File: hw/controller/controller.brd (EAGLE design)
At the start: 45 x 45 mm, 99 parts, among them J1 JST-PH3SMT_VERT, J2 JST-PH3SMT_VERT, M3 PAD24AWG_PAD, Q1 TPN1R603PL, Q2 TPN1R603PL, Q3 TPN1R603PL, Q4 TPN1R603PL, Q5 TPN1R603PL, Q6 TPN1R603PL, U1 STM32F4R_64PIN, U2 DRV8323RS, U3 AS5147, U4 MAX13431E, U5 MAX13433EETD+T, X1 8.0MHz

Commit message: controller: Officially switch to 500mOhm sense resistor
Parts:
- RA, RB, RC: value 1mOhm 1% 2W -> 0.5mOhm 1% 2W
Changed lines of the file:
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@@
 <attribute name="MF" value="Samsung Electro-Mechanics" x="26.9" y="25.9" size="1.778" layer="27" display="off"/>
 </element>
-<element name="RA" library="rcl" package="M1206" value="1mOhm 1% 2W" x="18.2" y="9.6" smashed="yes" rot="R270">
+<element name="RA" library="rcl" package="M1206" value="0.5mOhm 1% 2W" x="18.2" y="9.6" smashed="yes" rot="R270">
 <attribute name="MF" value="Stackpole Electronics" x="18.2" y="9.6" size="1.778" layer="27" rot="R270" display="off"/>
-<attribute name="MPN" value="HCS1206FT1L00" x="18.2" y="9.6" size="1.778" layer="27" rot="R270" display="off"/>
+<attribute name="MPN" value="HCS1206FTL500" x="18.2" y="9.6" size="1.778" layer="27" rot="R270" display="off"/>
 <attribute name="NAME" x="18.770003125" y="7.23" size="0.6096" layer="25" font="vector" ratio="10" rot="R180"/>
 <attribute name="POPULATE" value="1" x="18.2" y="9.6" size="1.778" layer="27" rot="R270" display="off"/>
@@
 <attribute name="POPULATE" value="0" x="33.63" y="12.03" size="1.778" layer="27" rot="R90" display="off"/>
 </element>
-<element name="RB" library="rcl" package="M1206" value="1mOhm 1% 2W" x="21.4" y="9.6" smashed="yes" rot="R270">
-<attribute name="MPN" value="HCS1206FT1L00" x="21.4" y="9.6" size="1.778" layer="27" rot="R270" display="off"/>
+<element name="RB" library="rcl" package="M1206" value="0.5mOhm 1% 2W" x="21.4" y="9.6" smashed="yes" rot="R270">
+<attribute name="MPN" value="HCS1206FTL500" x="21.4" y="9.6" size="1.778" layer="27" rot="R270" display="off"/>
 <attribute name="MF" value="Stackpole Electronics" x="21.4" y="9.6" size="1.778" layer="27" rot="R270" display="off"/>
 <attribute name="NAME" x="22.070003125" y="7.23" size="0.6096" layer="25" font="vector" ratio="10" rot="R180"/>
 <attribute name="POPULATE" value="1" x="21.4" y="9.6" size="1.778" layer="27" rot="R270" display="off"/>
 </element>
-<element name="RC" library="rcl" package="M1206" value="1mOhm 1% 2W" x="34.5" y="9.6" smashed="yes" rot="R270">
-<attribute name="MPN" value="HCS1206FT1L00" x="34.5" y="9.6" size="1.778" layer="27" rot="R270" display="off"/>
+<element name="RC" library="rcl" package="M1206" value="0.5mOhm 1% 2W" x="34.5" y="9.6" smashed="yes" rot="R270">
+<attribute name="MPN" value="HCS1206FTL500" x="34.5" y="9.6" size="1.778" layer="27" rot="R270" display="off"/>
 <attribute name="MF" value="Stackpole Electronics" x="34.5" y="9.6" size="1.778" layer="27" rot="R270" display="off"/>
 <attribute name="NAME" x="35.17" y="7.229996875" size="0.6096" layer="25" ratio="10" rot="R180"/>

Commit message: controller: Transcribe r3.1 part selection back into eagle
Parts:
- C12, C23, C24, C25, C27, C28, C29, C30: value 1uF 35V -> 1.5uF 35V

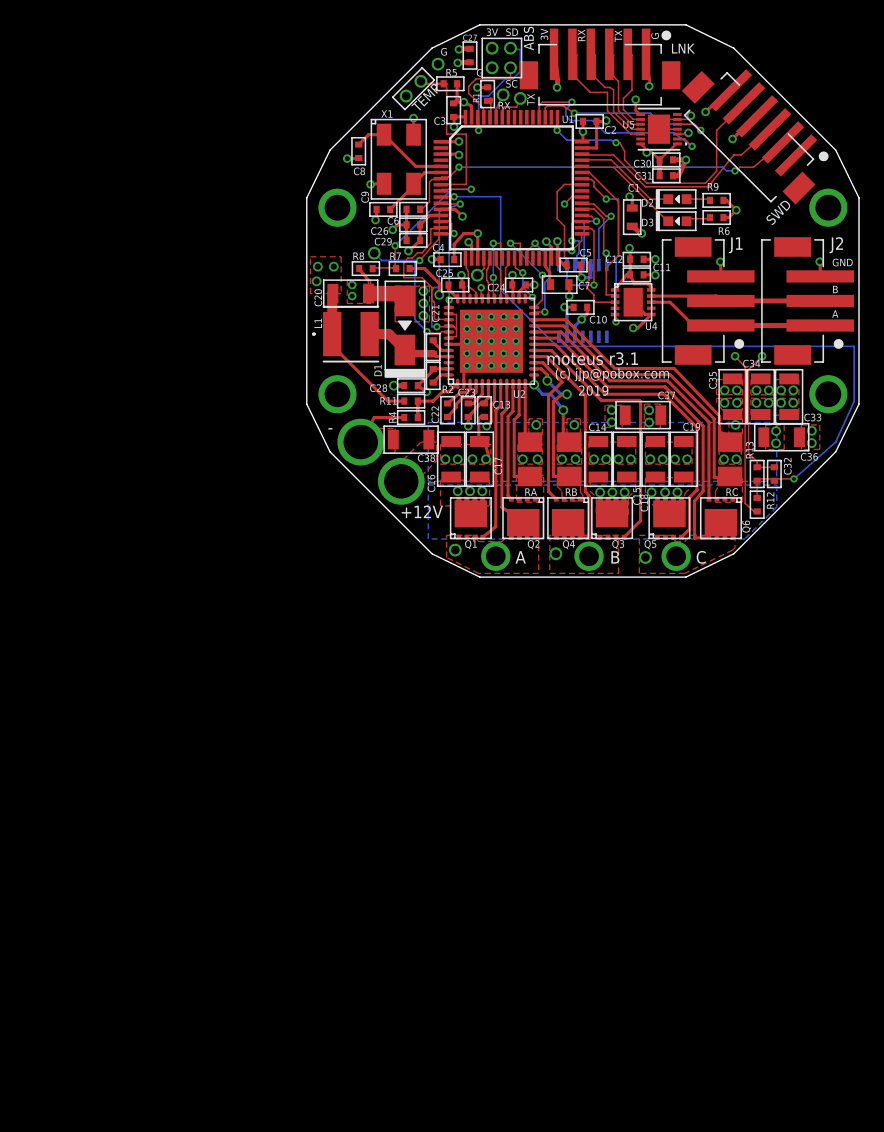
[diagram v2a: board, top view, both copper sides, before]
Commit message: Work on r4 of controller
Parts are in place, but part names are bogus, silks haven't been
placed, and auto-routing not done yet.
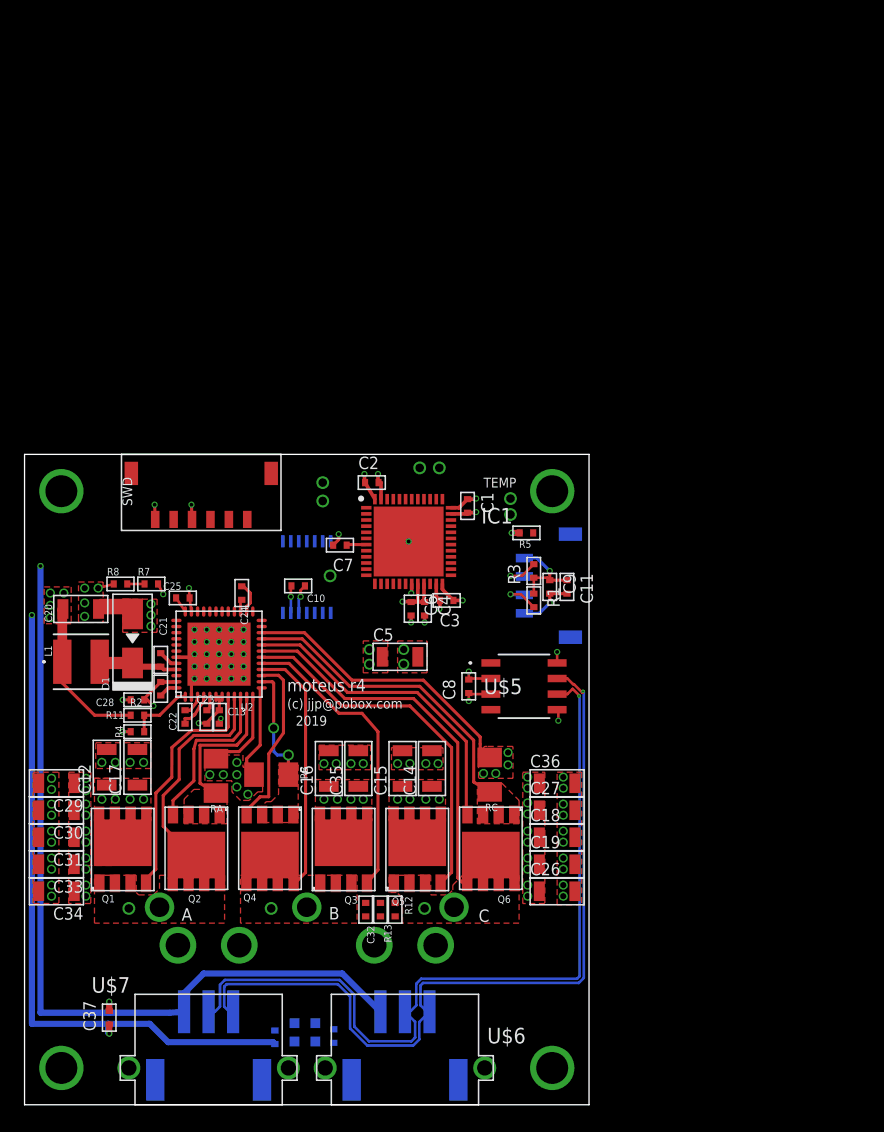
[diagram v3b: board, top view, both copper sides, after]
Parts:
- removed ABS_3V, ABS_GND, ABS_SCL, ABS_SDA, DAC1, DGND, DRX, DTX, M3: PAD24AWG_PAD, controller:24AWG_PAD
- removed C38: 10uF, mfpassives:C1206
- removed J1, J2: JST-PH3SMT_VERT, controller:JST_B3B_PH-SM4-TB(LF)(SN)
- removed LNK: JST-ZH6SMT_VERT, controller:JST_B6B-ZR-SM4-TF(LF)(SN)
- removed U1: STM32F4R_64PIN, controller:LQFP64
- removed U4: MAX13431E, controller:TDFN10
- removed U5: MAX13433EETD+T, controller:21-0137I_T1433-1
- removed V+, V-: PAD12AWG_PAD, controller:12AWG_PAD
- removed X1: 8.0MHz, controller:ABM3B
- added IC1: STM32G474CEU6, controller:QFN50P700X700X60-49N
- added R3: 2k, mfpassives:R0402
- added U$10, U$11: JST-PH3, controller:JST_S3B-PH-SM4-TB(LF)(SN)
- added U$12, U$13, U$14, U$9: MOUNT, controller:M2.5MOUNT
- added U$15: PAD24AWG_PAD, controller:24AWG_PAD
- added U$5: TCAN334G, controller:SOT23-8
- added U$6, U$7: XT30XT30PW_MALE, controller:XT30PW_MALE
- added U$8: JST_ZH4, controller:JST_S4B-ZR-SM4A-TF(LF)(SN)
- C1, C7: value 4.7uF -> 0.1uF 50V; device mfpassives:C0603 -> mfpassives:C0402
- C12, C27, C29, C30: value 1.5uF 35V -> 10uF; device mfpassives:C0402 -> mfpassives:C1206
- C26, C31, C5: value 0.1uF 50V -> 10uF; device mfpassives:C0402 -> mfpassives:C1206
- C37: value 10uF -> 0.1uF 50V; device mfpassives:C1206 -> mfpassives:C0402
- C6: value 0.1uF 50V -> 1uF
- C8: value 10pF -> 0.1uF 50V
- C9: value 10pF -> 1uF
- Q1, Q2, Q3, Q4, Q5, Q6: value TPN1R603PL -> TPH1R204PLSOP_ADVANCE_8; device controller:TSON_ADVANCE_8 -> controller:SOP_ADVANCE_8
- R1: value 220 -> 2k
- SWD: value JST-ZH6SMT_VERT -> JST-ZH6; device controller:JST_B6B-ZR-SM4-TF(LF)(SN) -> controller:JST_S6B-ZR-SM4A-TF(LF)(SN)
- U$1, U$2, U$3, U$4: value MOUNTM2 -> PAD24AWG_PAD; device controller:M2MOUNT -> controller:24AWG_PAD
- moved R6 75.9 mm to (-2.60, -37.5), flipped to the bottom, turned to 90 degrees
- moved R9 74.9 mm to (2.20, -37.4), flipped to the bottom, turned to 90 degrees
- moved D2 74.0 mm to (0.70, -37.1), flipped to the bottom, turned to 270 degrees
- moved C31 73.3 mm to (-20.4, -21.2), turned to 180 degrees
- moved D3 73.1 mm to (-1.00, -37.1), flipped to the bottom, turned to 270 degrees
- moved C30 72.7 mm to (-20.4, -19.0), turned to 180 degrees
- moved C33 70.8 mm to (-20.4, -23.4), turned to 180 degrees
- moved C34 70.1 mm to (-20.4, -25.6), turned to 180 degrees
- moved C37 65.6 mm to (-16.1, -35.9), turned to 90 degrees
- moved C27 61.9 mm to (20.4, -19.0), turned to 0 degrees
- moved C12 59.8 mm to (-16.3, -15.5), turned to 90 degrees
- moved C26 55.6 mm to (20.4, -25.6), turned to 0 degrees
- moved SWD 54.1 mm to (-8.60, 4.70), turned to 0 degrees
- moved C29 52.9 mm to (-20.4, -16.8)
- moved C32 48.7 mm to (4.80, -27.1), turned to 270 degrees
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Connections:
- removed net AS5047_I: U3.14
- removed net DBG_A: LNK.5, U5.12
- removed net DBG_B: LNK.4, U5.11
- removed net DBG_Y: LNK.2, U5.9
- removed net DBG_Z: LNK.3, U5.10
- removed net N$1: DAC1.P$1, U1.20
- removed net N$15: J1.1, J2.1, U4.8
- removed net N$2: DTX.P$1, U1.58
- removed net N$23: C7.P$1, U1.30
- removed net N$24: C6.P$1, SWD.2, U1.7
- removed net N$3: DRX.P$1, U1.59
- removed net N$33: R1.P$2, U1.60
- removed net N$35: C8.P$1, U1.5, X1.1
- removed net N$36: C9.P$1, U1.6, X1.3
- removed net N$6: SWD.5, U1.49
- removed net N$7: SWD.3, U1.46
- removed net N$9: J1.2, J2.2, U4.9
- removed net RS485_DIR: U1.41, U4.3, U4.4
- removed net RS485_RX: U1.43, U4.2
- removed net RS485_TX: U1.42, U4.5
- new net CAN_N: U$10.2, U$11.2, U$5.6
- new net CAN_P: U$10.1, U$11.1, U$5.7
- new net CAN_RX: IC1.33, U$5.4
- new net CAN_TX: IC1.34, U$5.1
- new net DAC: IC1.12, U$15.P$1
- new net DEBUG1: IC1.5, U$3.P$1
- new net DEBUG2: IC1.6, U$4.P$1
- new net NRST: C7.P$1, IC1.7, SWD.2
- new net SWCLK: IC1.38, SWD.5
- new net SWDIO: IC1.37, SWD.3
- net +3V3: now also C37.P$1, C5.P$2, C6.P$1, C8.P$1, C9.P$1, IC1.20, IC1.21, IC1.24, IC1.36, IC1.48, R1.P$1, R3.P$1, U$5.3, U$8.1; no longer ABS_3V.P$1, C12.P$1, C26.P$1, C27.P$1, C29.P$1, C30.P$1, C31.P$1, C5.P$1, LNK.6, U1.1, U1.13, U1.19, U1.32, U1.48, U1.64, U4.1, U4.10, U5.1, U5.14, U5.3
- net AS5047_A: now also IC1.42; no longer U1.37
- net AS5047_B: now also IC1.41; no longer U1.38
- net AS5047_CS: now also IC1.25; no longer U1.33
- net AS5047_MISO: now also IC1.28; no longer U1.35
- net AS5047_MOSI: now also IC1.29; no longer U1.36
- net AS5047_SCK: now also IC1.27; no longer U1.34
- net CUR1: now also IC1.16; no longer U1.25
- net CUR2: now also IC1.17; no longer U1.26
- net CUR3: now also IC1.18; no longer U1.27
- net DEBUG_RX: now also IC1.39, U$2.P$1; no longer U1.52, U5.2
- net DEBUG_TX: now also IC1.40, U$1.P$1; no longer U1.51, U5.5
- net DRV8323_CS: now also IC1.2; no longer U1.39
- net DRV8323_MISO: now also IC1.14; no longer U1.22
- net DRV8323_MOSI: now also IC1.15; no longer U1.23
- net DRV8323_SCLK: now also IC1.13; no longer U1.21
- net GND: now also C37.P$2, C5.P$1, IC1.19, IC1.23, IC1.35, IC1.47, IC1.49, U$10.3, U$11.3, U$5.2, U$5.5, U$5.8, U$8.4; no longer ABS_GND.P$1, C12.P$2, C26.P$2, C27.P$2, C29.P$2, C30.P$2, C31.P$2, C5.P$2, DGND.P$1, J1.3, J2.3, LNK.1, R1.P$1, U1.12, U1.18, U1.3, U1.31, U1.47, U1.63, U4.6, U4.PAD, U5.15, U5.4, U5.6, U5.8, X1.2, X1.4
- net I2C_ABS_SCL: now also IC1.45, R3.P$2, U$8.2; no longer ABS_SCL.P$1, U1.61
- net I2C_ABS_SDA: now also IC1.46, R1.P$2, U$8.3; no longer ABS_SDA.P$1, U1.62
- net LED1: now also IC1.4; no longer U1.44
- net LED2: now also IC1.3; no longer U1.45
- net MOTOR1: now also IC1.8; no longer U1.14
- net MOTOR2: now also IC1.9; no longer U1.15
- net MOTOR3: now also IC1.10; no longer M3.P$1, U1.16
- net MOTOR_ENABLE: now also IC1.11; no longer U1.17
- net MOTOR_FAULT: now also IC1.43; no longer U1.24
- net MOTOR_HIZ: now also IC1.44; no longer U1.11
- net V+: now also C12.P$1, C26.P$1, C27.P$1, C29.P$1, C30.P$1, C31.P$1, U$6.1, U$7.1; no longer C37.P$1, C38.P$1, V+.1
- net V-: now also C12.P$2, C26.P$2, C27.P$2, C29.P$2, C30.P$2, C31.P$2, U$6.2, U$7.2; no longer C37.P$2, C38.P$2, V-.1
- net VBAT_SENSE: now also IC1.30; no longer U1.9
- net VTEMP_FET: now also IC1.31; no longer U1.10
- net VTEMP_MOT: now also IC1.26; no longer U1.8
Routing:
- net CAN_P: track 0.00 -> 67.1 mm, vias 0 -> 1
- net CAN_N: track 0.00 -> 66.8 mm, vias 0 -> 1
- net VTEMP_FET: track 60.6 -> 0.00 mm, vias 2 -> 0
- net N$24: track 32.9 -> 0.00 mm, vias 2 -> 0
- net +3V3: track 71.7 -> 96.5 mm, vias 20 -> 16
- net N$6: track 23.3 -> 0.00 mm, vias 2 -> 0
- net GND: track 75.1 -> 96.5 mm, vias 33 -> 24
- net MOTOR_HIZ: track 18.6 -> 0.00 mm, vias 2 -> 0
- net N$7: track 18.4 -> 0.00 mm
- net DEBUG_RX: track 17.7 -> 0.00 mm, vias 2 -> 0
- net DEBUG_TX: track 16.4 -> 0.00 mm, vias 2 -> 0
- net RS485_DIR: track 16.0 -> 0.00 mm
- net MOTOR3: track 15.2 -> 0.00 mm, vias 2 -> 0
- net RS485_TX: track 14.6 -> 0.00 mm, vias 2 -> 0
- net N$15: track 14.6 -> 0.00 mm
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- removed copper zone on layer 16, net V+
- removed copper zone on layer 16, net V-
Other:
- board size 45 x 45 mm -> 46 x 53 mm
- board text added: "moteus r4"
- board text removed: "+12V"
- board text removed: "-"
- board text removed: "3V"
- board text removed: "ABS"
- board text removed: "G"
- board text removed: "GND"
- board text removed: "RX"
- board text removed: "SC"
- board text removed: "SD"
- board text removed: "TX"
- board text removed: "moteus r3.1"

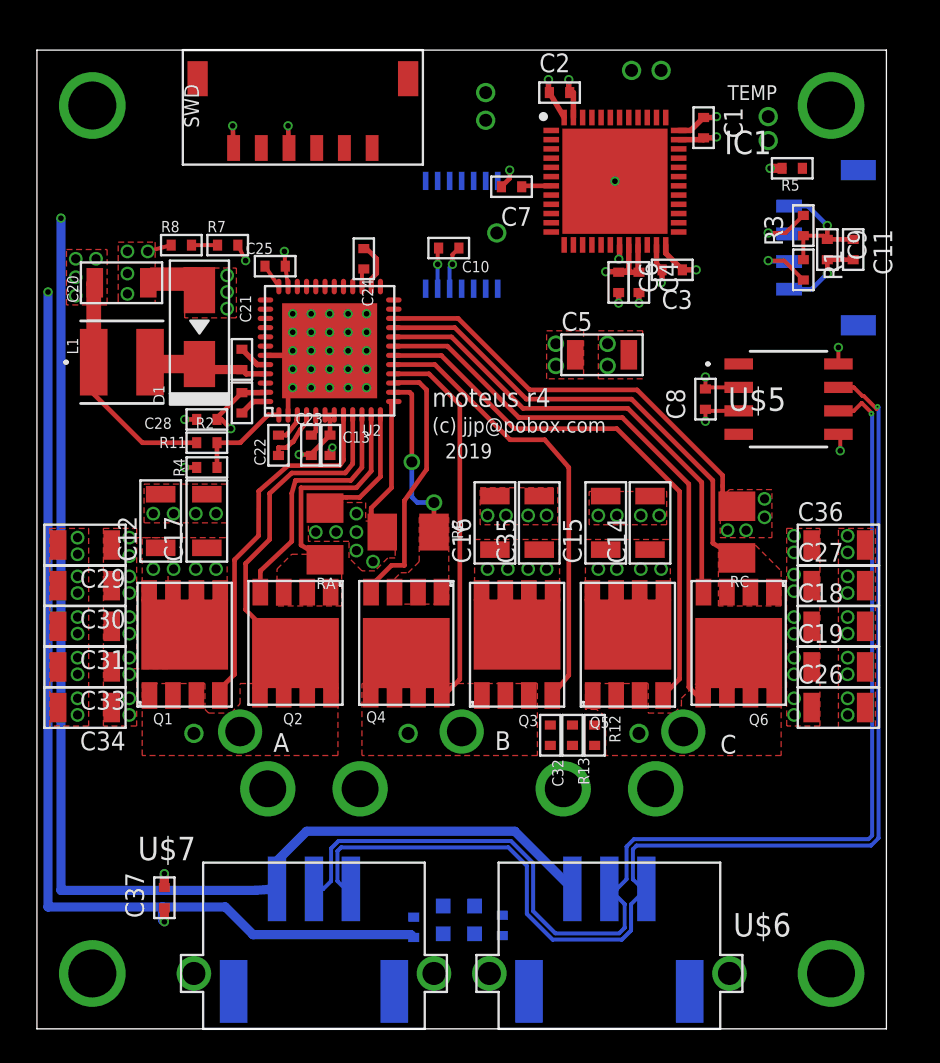
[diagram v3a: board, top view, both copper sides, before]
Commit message: Add parts roughly placed and named
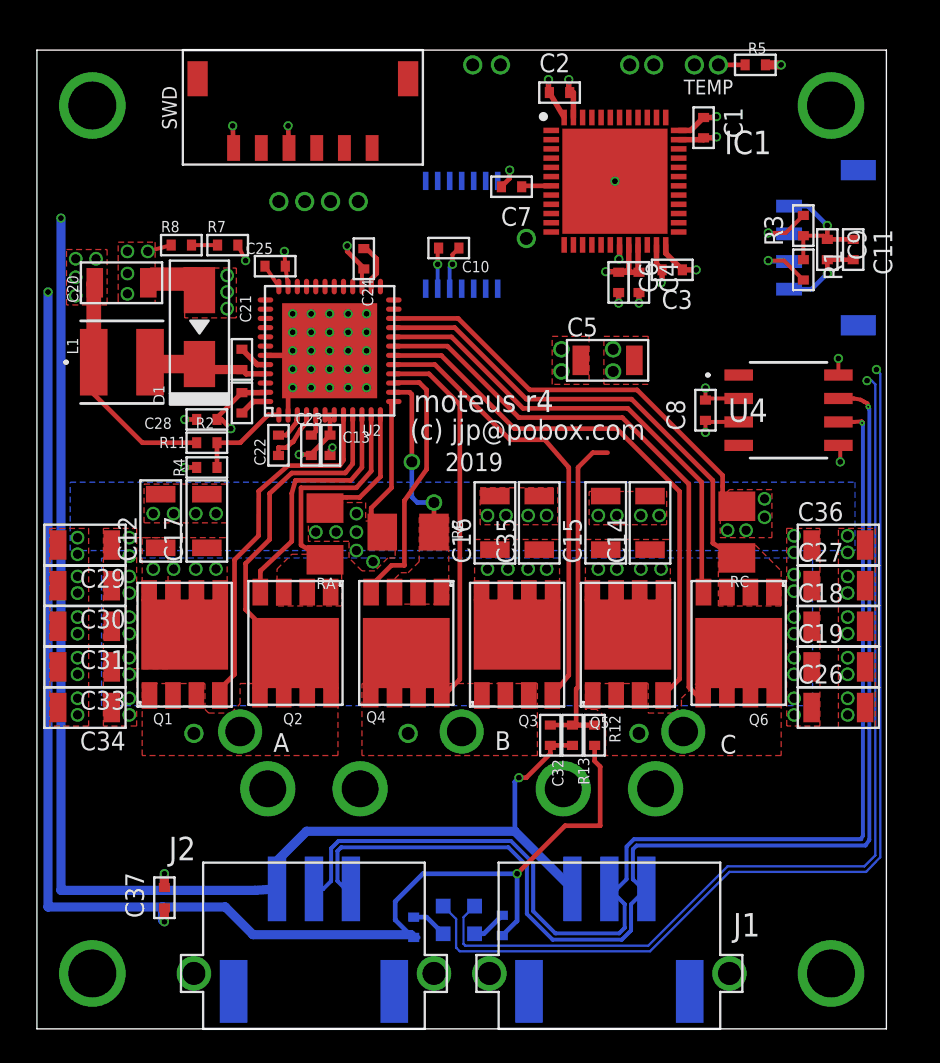
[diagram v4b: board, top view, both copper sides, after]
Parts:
- removed U$1, U$15, U$2, U$3, U$4: PAD24AWG_PAD, controller:24AWG_PAD
- removed U$5: TCAN334G, controller:SOT23-8
- added DAC, DBG1, DBG2, DRV_CS, DRV_MISO, DRV_MOSI, DRV_SCK, DTR, DTX: PAD24AWG_PAD, controller:24AWG_PAD
- added U4: TCAN334G, controller:SOT23-8
- moved R5 5.95 mm to (15.9, 9.20), turned to 0 degrees
- moved TEMP2 4.91 mm to (13.9, 9.20)
- moved TEMP1 4.88 mm to (12.6, 9.20)
- moved C8 0.60 mm to (13.2, -9.50)
- moved C5 0.42 mm to (7.90, -6.80)
- renumbered U$10 to CAN1, U$11 to CAN2, U$6 to J1, U$7 to J2, U$8 to ABS
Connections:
- net +3V3: now also U4.3; no longer U$5.3
- net CAN_N: now also U4.6; no longer U$5.6
- net CAN_P: now also U4.7; no longer U$5.7
- net CAN_RX: now also U4.4; no longer U$5.4
- net CAN_TX: now also U4.1; no longer U$5.1
- net DAC: now also DAC.P$1; no longer U$15.P$1
- net DEBUG1: now also DBG1.P$1; no longer U$3.P$1
- net DEBUG2: now also DBG2.P$1; no longer U$4.P$1
- net DEBUG_RX: now also DTR.P$1; no longer U$2.P$1
- net DEBUG_TX: now also DTX.P$1; no longer U$1.P$1
- net DRV8323_CS: now also DRV_CS.P$1
- net DRV8323_MISO: now also DRV_MISO.P$1
- net DRV8323_MOSI: now also DRV_MOSI.P$1
- net DRV8323_SCLK: now also DRV_SCK.P$1
- net GND: now also U4.2, U4.5, U4.8; no longer U$5.2, U$5.5, U$5.8
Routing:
- net LED1: track 0.00 -> 54.3 mm, vias 0 -> 1
- net LED2: track 0.00 -> 52.8 mm, vias 0 -> 1
- net +3V3: track 96.5 -> 120.1 mm, vias 16 -> 17
- net VTEMP_FET: track 0.00 -> 19.3 mm
- net GND: track 96.5 -> 105.2 mm, vias 24 -> 26
- net N$17: track 0.00 -> 1.97 mm
- net N$18: track 0.00 -> 1.91 mm
- net CAN_N: track 66.8 -> 64.9 mm
- net VTEMP_MOT: track 0.00 -> 1.45 mm
- net CAN_P: track 67.1 -> 65.8 mm
- added copper zone on layer 16, net V+
- added copper zone on layer 16, net V-
